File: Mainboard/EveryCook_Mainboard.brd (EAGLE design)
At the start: 103.1 x 103.7 mm, 110 parts, among them IC1 LM386MM-1, IC2 ATMEGA644A, Q1 8 MHz, Q2 BSP372, Q3 BSP372, T2 ZDT6790, U1 AD7794BRUZ, U4 78M05, U7 CJ1117-3.3

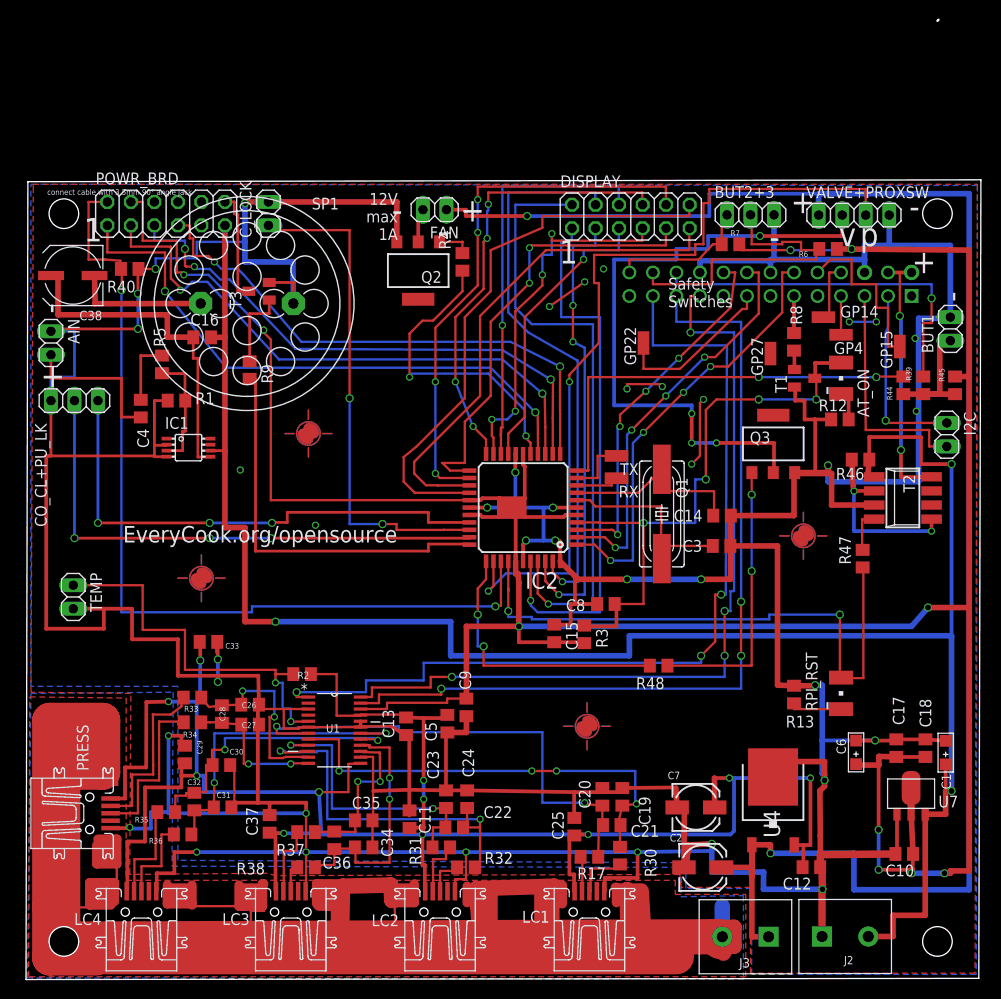
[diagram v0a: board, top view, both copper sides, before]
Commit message: Redesign of mainboard. New load cell amp board.
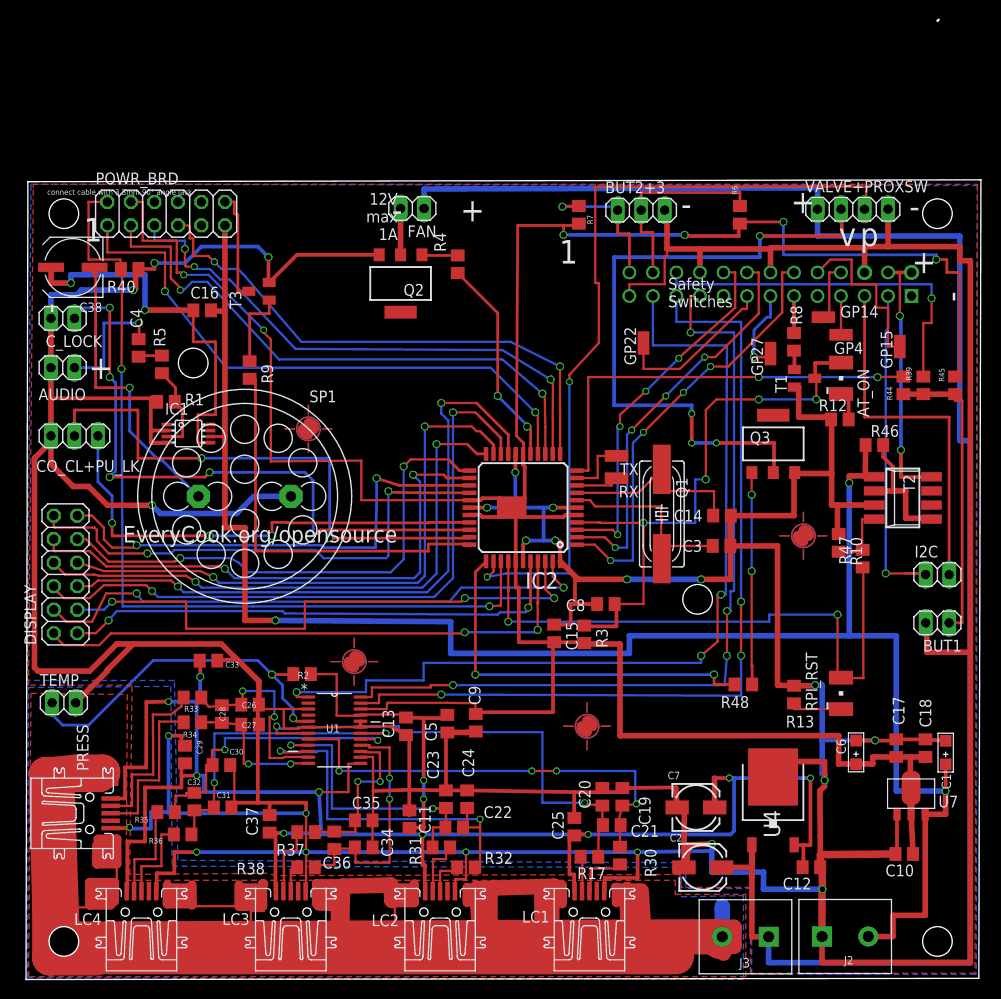
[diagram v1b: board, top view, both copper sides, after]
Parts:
- removed AIN: (no value), pinhead:1X02
- added AUDIO: (no value), pinhead:1X02
- added R10: 10k, rcl:R0805
- moved DISPLAY 72.3 mm to (4.37, 39.8), turned to 90 degrees
- moved BUT1 31.8 mm to (98.6, 34.5), turned to 180 degrees
- moved C_LOCK 24.9 mm to (4.06, 67.4), turned to 180 degrees
- moved SP1 20.8 mm to (23.7, 48.2)
- moved U$2 18.8 mm to (35.6, 30.4)
- moved R7 16.7 mm to (59.8, 78.6), turned to 90 degrees
- moved I2C 15.1 mm to (98.6, 39.8), turned to 180 degrees
- moved BUT2+3 11.8 mm to (66.5, 79.1)
- moved TEMP 11.5 mm to (4.19, 25.9), turned to 0 degrees
- moved R6 10.2 mm to (77.2, 78.6), turned to 90 degrees
- moved R48 9.37 mm to (77.6, 27.9)
- moved C4 6.56 mm to (12.3, 64.2), turned to 90 degrees
- moved CO_CL+PU_LK 3.81 mm to (5.33, 54.7)
- moved C16 2.92 mm to (19.1, 68.3)
- moved FAN 2.42 mm to (41.8, 79.3)
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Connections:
- net GND: now also AUDIO.1, R10.1; no longer AIN.1
- net N$27: now also AUDIO.2; no longer AIN.2
- net N$71: now also R10.2
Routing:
- net GND: track 756.6 -> 819.3 mm, vias 39 -> 23
- net PC0: track 31.6 -> 71.0 mm, vias 1 -> 2
- net PC1: track 44.3 -> 71.6 mm, vias 1 -> 2
- net PC2: track 40.1 -> 63.8 mm, vias 4 -> 2
- net +3V3: track 335.1 -> 314.8 mm, vias 10 -> 6
- net N$66: track 14.2 -> 32.5 mm
- net N$23: track 14.5 -> 31.8 mm, vias 0 -> 1
- net N$60: track 54.6 -> 69.6 mm, vias 2 -> 5
- net N$1: track 25.0 -> 39.2 mm
- net PC3: track 48.6 -> 62.8 mm, vias 4 -> 2
- net N$6: track 20.4 -> 34.5 mm
- net +5V: track 210.1 -> 197.1 mm
- net N$63: track 34.9 -> 22.0 mm
- net PB2: track 50.2 -> 62.2 mm
- net N$65: track 30.2 -> 41.8 mm
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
